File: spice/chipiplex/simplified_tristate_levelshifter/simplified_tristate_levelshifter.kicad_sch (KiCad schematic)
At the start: 23 parts, among them Q1 NPN, Q2 PNP, Q3 PNP, Q4 NPN

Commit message: Worked on simulations.
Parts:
- added R16: 400, symbol Device:R
- R10: value 200 -> 400
- R11: value 1 -> 200
- R15: value 1Meg -> 100k
- R5, R6: value 330 -> 100
- R7, R8: value 1k -> 2k
- renumbered Q2 to Q1, Q1 to Q2
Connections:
- net VIN: now also R9.2
- net VOUT: now also R16.2; no longer R11.1
- net VRev: no longer R11.2
- net at R9.1: now also V3.1
- net PWR3V3: now reaches R12.1, R15.1, V1.1
- net PWR5V: now reaches R13.1, V2.1
- net PWR5V: now also R16.1
- net Q3E: now reaches Q3.3 (E), R13.2, R7.1
- net Q1C renamed Q1C4B
- net Q2C renamed Q2C3B
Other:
- note added: "Lower R5 from 330 to 50 for better sinking ability"
- moved on the sheet: R11, R9

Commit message: Worked on levelshifter simulation.
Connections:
- net VOUT: now also R10.1; no longer R16.2
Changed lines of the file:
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@@
   (junction (at 104.14 110.49) (diameter 0) (color 0 0 0 0)
   )
+  (junction (at 104.267 62.738) (diameter 0) (color 0 0 0 0)
+  )
   (junction (at 163.83 96.52) (diameter 0) (color 0 0 0 0)
   )
-  (junction (at 104.267 62.738) (diameter 0) (color 0 0 0 0)
-  )
   (wire (pts (xy 104.14 106.68) (xy 104.14 110.49))
     (stroke (width 0) (type default))
@@
     (stroke (width 0) (type default))
   )
+  (wire (pts (xy 163.83 96.52) (xy 163.83 98.552))
+    (stroke (width 0) (type default))
+  )
   (wire (pts (xy 209.55 109.22) (xy 209.55 111.76))
     (stroke (width 0) (type default))
@@
     (stroke (width 0) (type default))
   )
+  (wire (pts (xy 163.83 96.52) (xy 185.928 96.52))
+    (stroke (width 0) (type default))
+  )
   (wire (pts (xy 114.3 88.9) (xy 114.3 94.996))
     (stroke (width 0) (type default))
@@
     (stroke (width 0) (type default))
   )
-  (wire (pts (xy 163.83 91.694) (xy 163.83 96.52))
-    (stroke (width 0) (type default))
-  )
   (wire (pts (xy 133.604 89.154) (xy 133.604 96.52))
     (stroke (width 0) (type default))
@@
   )
   (wire (pts (xy 104.267 62.738) (xy 104.14 62.738))
-    (stroke (width 0) (type default))
-  )
-  (wire (pts (xy 163.83 96.52) (xy 185.928 96.52))
     (stroke (width 0) (type default))
   )
@@
   )
   (text "Lower R5 from 330 to 50 for better sinking ability"
-    (at 166.497 134.493 0)
+    (at 181.229 161.29 0)
     (effects (font (size 1.27 1.27)) (justify left bottom))
   )
@@
     (effects (font (size 1.27 1.27)) (justify left bottom))
   )
-  (label "VOUT" (at 142.24 96.52 0) (fields_autoplaced)
+  (label "VOUT" (at 138.43 96.52 0) (fields_autoplaced)
     (effects (font (size 1.27 1.27)) (justify left bottom))
   )
@@
     (effects (font (size 1.27 1.27)) (justify left bottom))
   )
-  (label "VIN" (at 86.36 96.52 0) (fields_autoplaced)
+  (label "VIN" (at 95.504 96.52 0) (fields_autoplaced)
     (effects (font (size 1.27 1.27)) (justify left bottom))
   )
@@
       (effects (font (size 1.27 1.27)) (justify left) hide)
     )
-    (property "Sim.Params" "pulse(0 3.3 0 50u 50u 25u 150u)" (at 29.21 107.8202 0)
-      (effects (font (size 1.27 1.27)) (justify left))
-    )
+    (property "Sim.Params" "pulse(0 3.3 0 50n 50n 75u 150u)" (at 29.21 107.8202 0)
+      (effects (font (size 1.27 1.27)) (justify left))
+    )

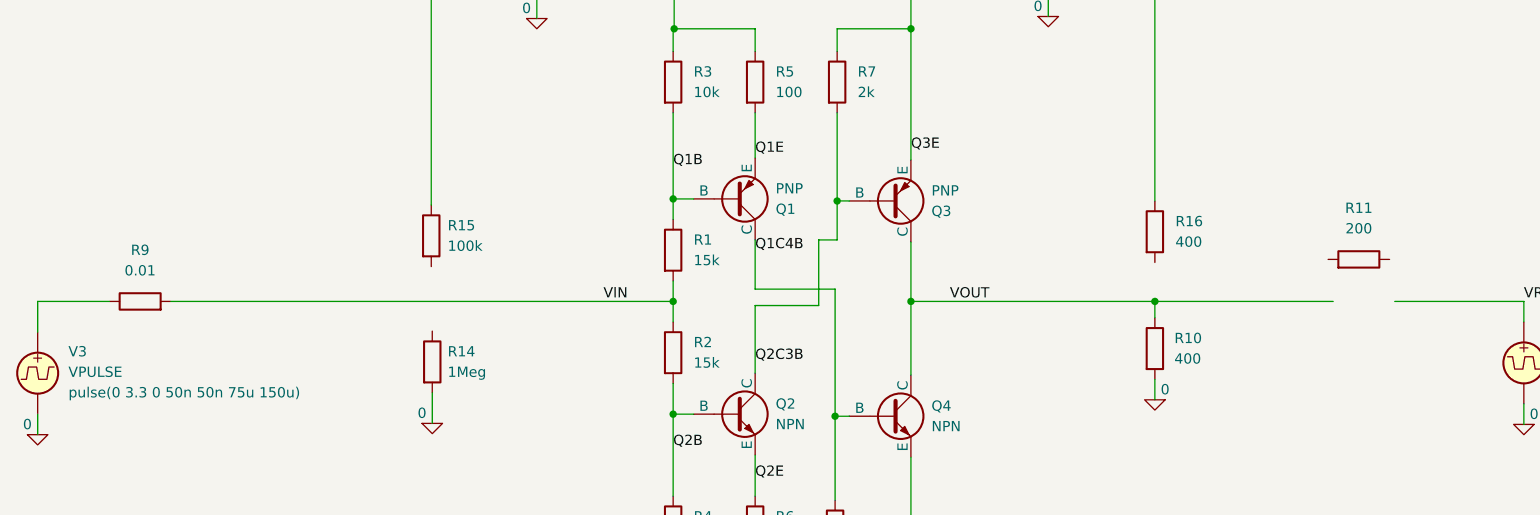
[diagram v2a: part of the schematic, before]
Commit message: Minor changes to spice sims.
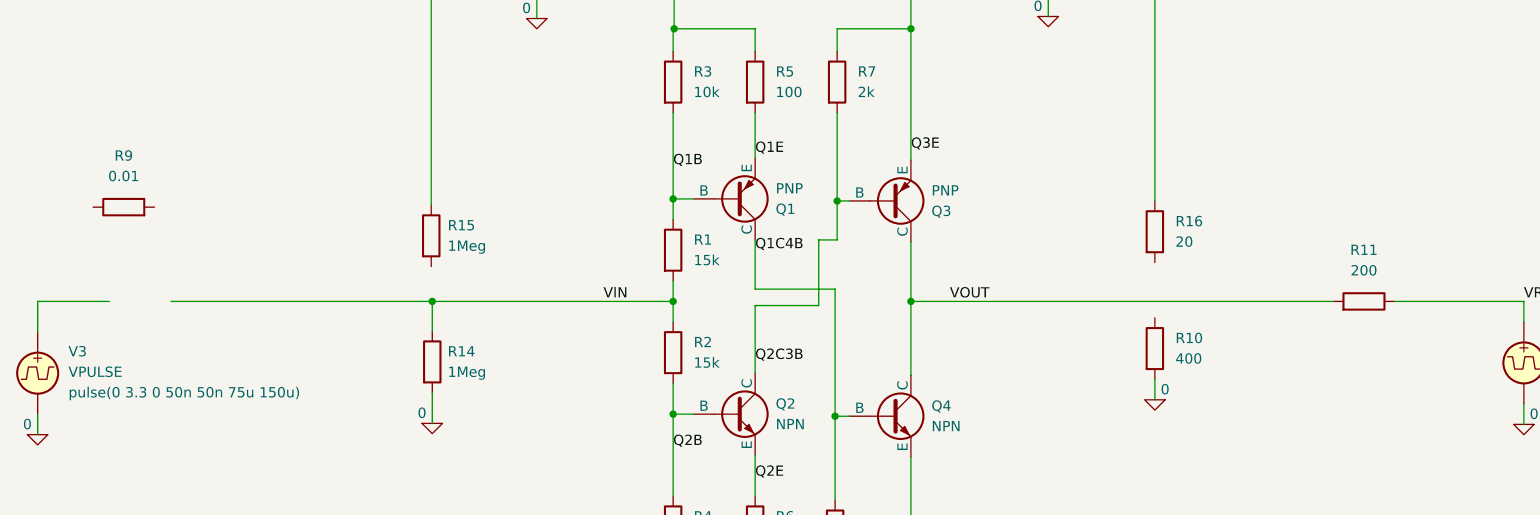
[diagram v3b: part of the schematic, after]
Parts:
- R15: value 100k -> 1Meg
- R16: value 400 -> 20
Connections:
- net VIN: now also R14.1; no longer R9.2
- net VOUT: now also R11.2; no longer R10.1
- net VRev: now also R11.1
- net at R9.1: no longer V3.1
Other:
- moved on the sheet: R11, R9
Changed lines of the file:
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@@
   (junction (at 133.604 62.738) (diameter 0) (color 0 0 0 0)
   )
+  (junction (at 74.295 96.52) (diameter 0) (color 0 0 0 0)
+  )
   (junction (at 104.14 110.49) (diameter 0) (color 0 0 0 0)
   )
   (junction (at 104.267 62.738) (diameter 0) (color 0 0 0 0)
   )
-  (junction (at 163.83 96.52) (diameter 0) (color 0 0 0 0)
-  )
   (wire (pts (xy 104.14 106.68) (xy 104.14 110.49))
     (stroke (width 0) (type default))
@@
     (stroke (width 0) (type default))
   )
+  (wire (pts (xy 41.91 96.52) (xy 74.295 96.52))
+    (stroke (width 0) (type default))
+  )
   (wire (pts (xy 124.206 94.996) (xy 124.206 110.744))
     (stroke (width 0) (type default))
   )
-  (wire (pts (xy 41.91 96.52) (xy 104.14 96.52))
-    (stroke (width 0) (type default))
-  )
   (wire (pts (xy 133.604 62.738) (xy 133.604 78.994))
     (stroke (width 0) (type default))
@@
     (stroke (width 0) (type default))
   )
-  (wire (pts (xy 163.83 96.52) (xy 163.83 98.552))
+  (wire (pts (xy 74.295 100.203) (xy 74.295 96.52))
     (stroke (width 0) (type default))
   )
@@
     (stroke (width 0) (type default))
   )
-  (wire (pts (xy 163.83 96.52) (xy 185.928 96.52))
-    (stroke (width 0) (type default))
-  )
   (wire (pts (xy 114.3 88.9) (xy 114.3 94.996))
     (stroke (width 0) (type default))
@@
     (stroke (width 0) (type default))
   )
+  (wire (pts (xy 74.295 96.52) (xy 104.14 96.52))
+    (stroke (width 0) (type default))
+  )
   (wire (pts (xy 163.83 106.172) (xy 163.83 108.712))
     (stroke (width 0) (type default))
@@
     (stroke (width 0) (type default))
   )
-  (wire (pts (xy 133.604 96.52) (xy 163.83 96.52))
+  (wire (pts (xy 133.604 96.52) (xy 185.928 96.52))
     (stroke (width 0) (type default))
   )
@@
     (effects (font (size 1.27 1.27)) (justify left bottom))
   )
-  (symbol (lib_id "Device:R") (at 38.1 96.52 90) (unit 1)
-    (in_bom yes) (on_board yes) (dnp no) (fields_autoplaced)
-    (property "Reference" "R9" (at 38.1 90.17 90)
-      (effects (font (size 1.27 1.27)))
-    )
-    (property "Value" "0.01" (at 38.1 92.71 90)
-      (effects (font (size 1.27 1.27)))
-    )
-    (property "Footprint" "" (at 38.1 98.298 90)
-      (effects (font (size 1.27 1.27)) hide)
-    )
-    (property "Datasheet" "~" (at 38.1 96.52 0)
+  (symbol (lib_id "Device:R") (at 36.068 84.836 90) (unit 1)
+    (in_bom yes) (on_board yes) (dnp no) (fields_autoplaced)
+    (property "Reference" "R9" (at 36.068 78.486 90)
+      (effects (font (size 1.27 1.27)))
+    )
+    (property "Value" "0.01" (at 36.068 81.026 90)
+      (effects (font (size 1.27 1.27)))
+    )
+    (property "Footprint" "" (at 36.068 86.614 90)
+      (effects (font (size 1.27 1.27)) hide)
+    )
+    (property "Datasheet" "~" (at 36.068 84.836 0)
       (effects (font (size 1.27 1.27)) hide)
     )
@@
   (symbol (lib_id "Device:R") (at 163.83 102.362 0) (unit 1)
     (in_bom yes) (on_board yes) (dnp no) (fields_autoplaced)
-    (property "Reference" "R10" (at 166.243 101.092 0)
-      (effects (font (size 1.27 1.27)) (justify left))
-    )
-    (property "Value" "400" (at 166.243 103.632 0)
+    (property "Reference" "R10" (at 166.37 101.092 0)
+      (effects (font (size 1.27 1.27)) (justify left))
+    )
+    (property "Value" "400" (at 166.37 103.632 0)
       (effects (font (size 1.27 1.27)) (justify left))
     )
@@
     )
   )
-  (symbol (lib_id "Device:R") (at 189.103 91.313 270) (mirror x) (unit 1)
-    (in_bom yes) (on_board yes) (dnp no) (fields_autoplaced)
-    (property "Reference" "R11" (at 189.103 84.963 90)
-      (effects (font (size 1.27 1.27)))
-    )
-    (property "Value" "200" (at 189.103 87.503 90)
-      (effects (font (size 1.27 1.27)))
-    )
-    (property "Footprint" "" (at 189.103 93.091 90)
-      (effects (font (size 1.27 1.27)) hide)
-    )
-    (property "Datasheet" "~" (at 189.103 91.313 0)
+  (symbol (lib_id "Device:R") (at 189.738 96.52 270) (mirror x) (unit 1)
+    (in_bom yes) (on_board yes) (dnp no) (fields_autoplaced)
+    (property "Reference" "R11" (at 189.738 90.17 90)
+      (effects (font (size 1.27 1.27)))
+    )
+    (property "Value" "200" (at 189.738 92.71 90)
+      (effects (font (size 1.27 1.27)))
+    )
+    (property "Footprint" "" (at 189.738 98.298 90)
+      (effects (font (size 1.27 1.27)) hide)
+    )
+    (property "Datasheet" "~" (at 189.738 96.52 0)
       (effects (font (size 1.27 1.27)) hide)
     )
@@
       (effects (font (size 1.27 1.27)) (justify left))
     )
-    (property "Value" "400" (at 166.37 89.154 0)
+    (property "Value" "20" (at 166.37 89.154 0)
       (effects (font (size 1.27 1.27)) (justify left))
     )
@@
       (effects (font (size 1.27 1.27)) (justify left))
     )
-    (property "Value" "100k" (at 76.2 89.662 0)
-      (effects (font (size 1.27 1.27)) (justify left))
-    )
+    (property "Value" "1Meg" (at 76.2 89.662 0)
+      (effects (font (size 1.27 1.27)) (justify left))
+    )

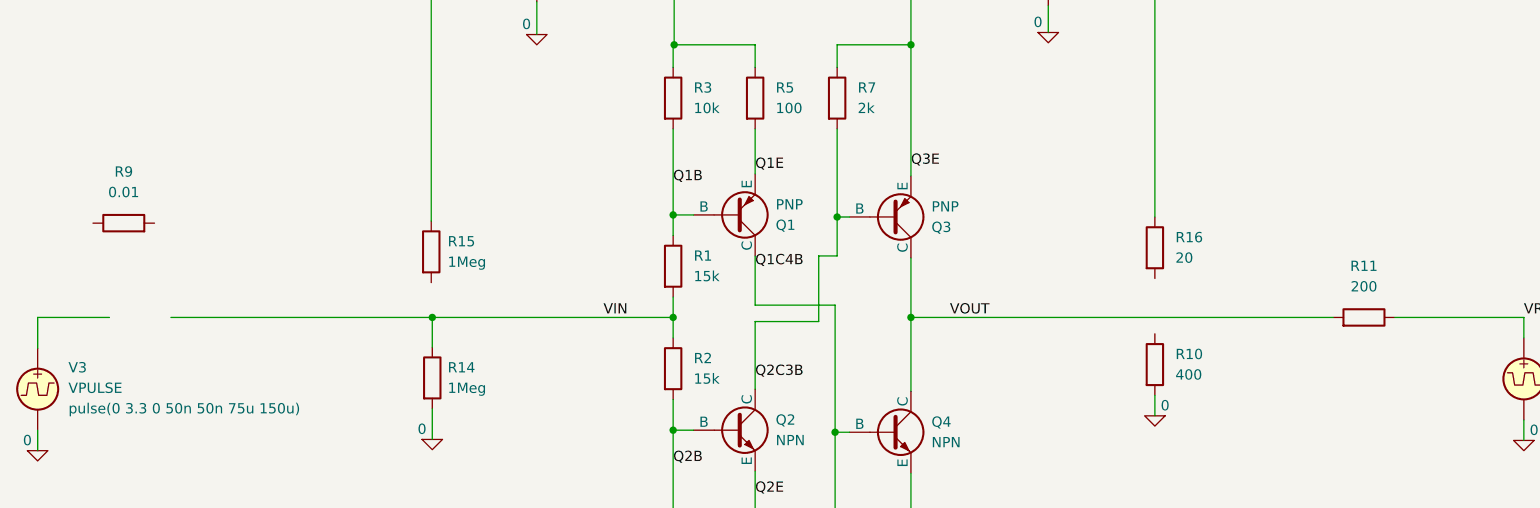
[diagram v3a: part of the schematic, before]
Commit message: Added transistor spice sims.
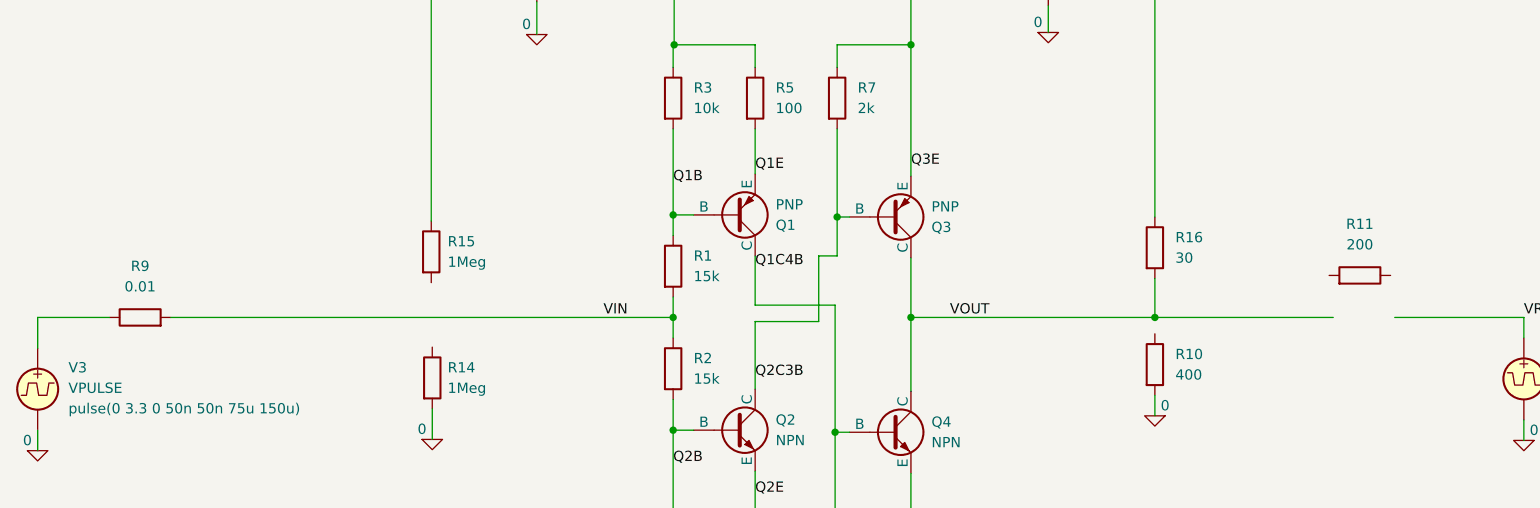
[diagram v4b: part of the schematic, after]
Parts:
- R16: value 20 -> 30
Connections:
- net VIN: now also R9.2; no longer R14.1
- net VOUT: now also R16.2; no longer R11.2
- net VRev: no longer R11.1
- net at R9.1: now also V3.1
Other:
- moved on the sheet: R11, R9
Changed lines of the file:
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@@
   (junction (at 124.206 130.81) (diameter 0) (color 0 0 0 0)
   )
+  (junction (at 163.83 96.52) (diameter 0) (color 0 0 0 0)
+  )
   (junction (at 133.604 96.52) (diameter 0) (color 0 0 0 0)
   )
@@
   (junction (at 133.604 62.738) (diameter 0) (color 0 0 0 0)
   )
-  (junction (at 74.295 96.52) (diameter 0) (color 0 0 0 0)
-  )
   (junction (at 104.14 110.49) (diameter 0) (color 0 0 0 0)
   )
@@
     (stroke (width 0) (type default))
   )
-  (wire (pts (xy 41.91 96.52) (xy 74.295 96.52))
-    (stroke (width 0) (type default))
-  )
   (wire (pts (xy 124.206 94.996) (xy 124.206 110.744))
     (stroke (width 0) (type default))
@@
     (stroke (width 0) (type default))
   )
-  (wire (pts (xy 74.295 100.203) (xy 74.295 96.52))
-    (stroke (width 0) (type default))
-  )
   (wire (pts (xy 209.55 109.22) (xy 209.55 111.76))
     (stroke (width 0) (type default))
@@
     (stroke (width 0) (type default))
   )
-  (wire (pts (xy 74.295 96.52) (xy 104.14 96.52))
+  (wire (pts (xy 163.83 96.52) (xy 185.928 96.52))
+    (stroke (width 0) (type default))
+  )
+  (wire (pts (xy 41.91 96.52) (xy 104.14 96.52))
     (stroke (width 0) (type default))
   )
@@
     (stroke (width 0) (type default))
   )
+  (wire (pts (xy 163.83 91.694) (xy 163.83 96.52))
+    (stroke (width 0) (type default))
+  )
   (wire (pts (xy 124.206 110.744) (xy 125.984 110.744))
     (stroke (width 0) (type default))
@@
     (stroke (width 0) (type default))
   )
-  (wire (pts (xy 133.604 96.52) (xy 185.928 96.52))
+  (wire (pts (xy 133.604 96.52) (xy 163.83 96.52))
     (stroke (width 0) (type default))
   )
@@
     (effects (font (size 1.27 1.27)) (justify left bottom))
   )
-  (symbol (lib_id "Device:R") (at 36.068 84.836 90) (unit 1)
-    (in_bom yes) (on_board yes) (dnp no) (fields_autoplaced)
-    (property "Reference" "R9" (at 36.068 78.486 90)
-      (effects (font (size 1.27 1.27)))
-    )
-    (property "Value" "0.01" (at 36.068 81.026 90)
-      (effects (font (size 1.27 1.27)))
-    )
-    (property "Footprint" "" (at 36.068 86.614 90)
-      (effects (font (size 1.27 1.27)) hide)
-    )
-    (property "Datasheet" "~" (at 36.068 84.836 0)
+  (symbol (lib_id "Device:R") (at 38.1 96.52 90) (unit 1)
+    (in_bom yes) (on_board yes) (dnp no) (fields_autoplaced)
+    (property "Reference" "R9" (at 38.1 90.17 90)
+      (effects (font (size 1.27 1.27)))
+    )
+    (property "Value" "0.01" (at 38.1 92.71 90)
+      (effects (font (size 1.27 1.27)))
+    )
+    (property "Footprint" "" (at 38.1 98.298 90)
+      (effects (font (size 1.27 1.27)) hide)
+    )
+    (property "Datasheet" "~" (at 38.1 96.52 0)
       (effects (font (size 1.27 1.27)) hide)
     )
@@
     )
   )
-  (symbol (lib_id "Device:R") (at 189.738 96.52 270) (mirror x) (unit 1)
-    (in_bom yes) (on_board yes) (dnp no) (fields_autoplaced)
-    (property "Reference" "R11" (at 189.738 90.17 90)
-      (effects (font (size 1.27 1.27)))
-    )
-    (property "Value" "200" (at 189.738 92.71 90)
-      (effects (font (size 1.27 1.27)))
-    )
-    (property "Footprint" "" (at 189.738 98.298 90)
-      (effects (font (size 1.27 1.27)) hide)
-    )
-    (property "Datasheet" "~" (at 189.738 96.52 0)
+  (symbol (lib_id "Device:R") (at 189.23 91.313 270) (mirror x) (unit 1)
+    (in_bom yes) (on_board yes) (dnp no) (fields_autoplaced)
+    (property "Reference" "R11" (at 189.23 84.963 90)
+      (effects (font (size 1.27 1.27)))
+    )
+    (property "Value" "200" (at 189.23 87.503 90)
+      (effects (font (size 1.27 1.27)))
+    )
+    (property "Footprint" "" (at 189.23 93.091 90)
+      (effects (font (size 1.27 1.27)) hide)
+    )
+    (property "Datasheet" "~" (at 189.23 91.313 0)
       (effects (font (size 1.27 1.27)) hide)
     )
@@
       (effects (font (size 1.27 1.27)) (justify left))
     )
-    (property "Value" "20" (at 166.37 89.154 0)
-      (effects (font (size 1.27 1.27)) (justify left))
-    )
+    (property "Value" "30" (at 166.37 89.154 0)
+      (effects (font (size 1.27 1.27)) (justify left))
+    )
